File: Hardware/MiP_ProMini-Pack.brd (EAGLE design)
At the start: 41.4 x 63.8 mm, 45 parts, among them Q1 8MHz, U1 ATMEGA328, U2 MIC5205, U3 TS3USB221A

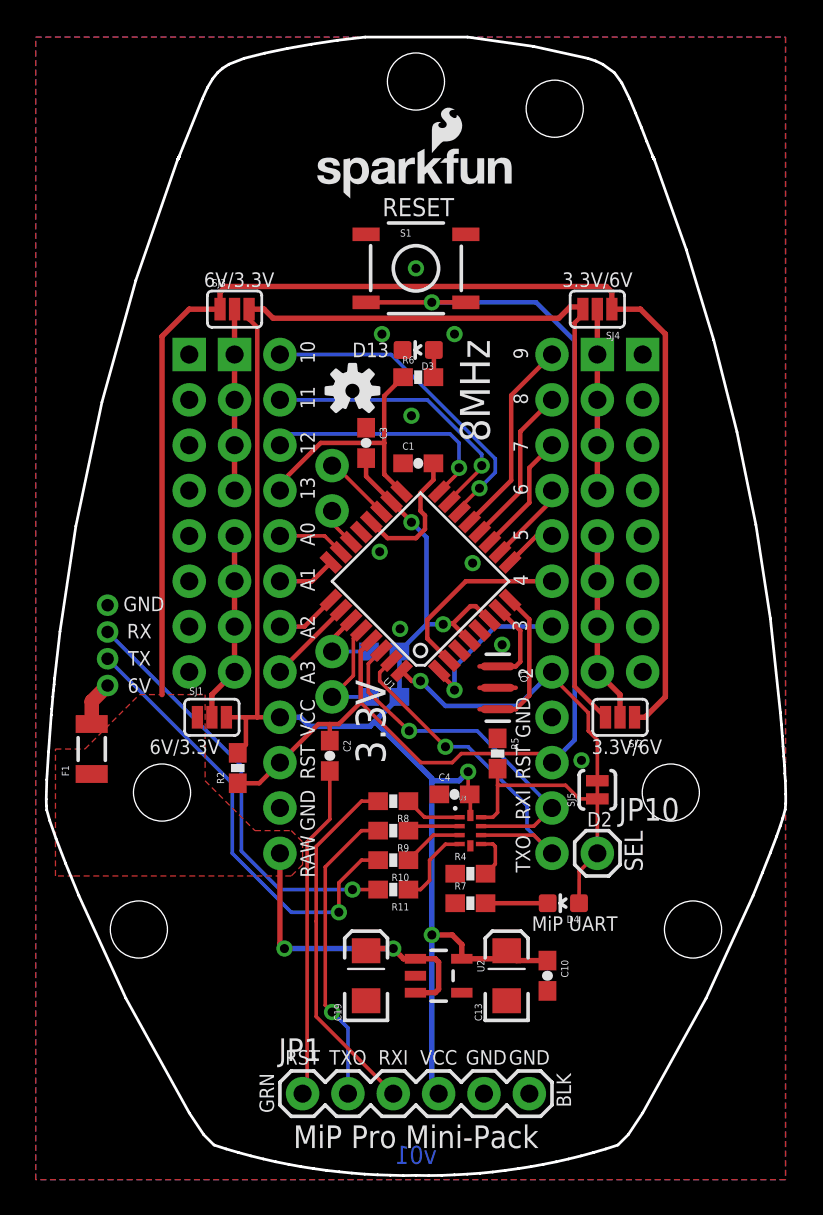
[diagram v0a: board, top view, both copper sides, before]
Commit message: moved components near screw holes. Gives more clearance for hardware
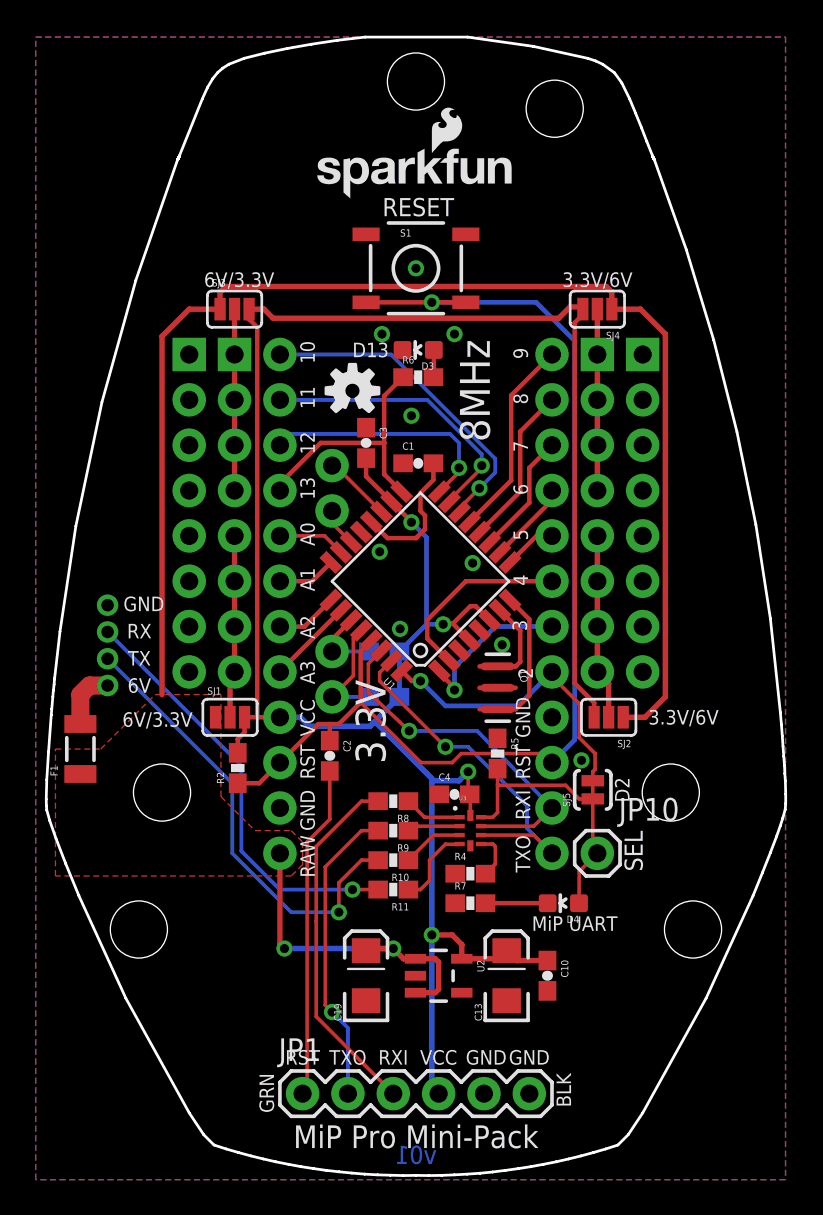
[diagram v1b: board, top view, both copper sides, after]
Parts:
- moved SJ1 1.02 mm to (10.9, 25.9)
- moved F1 0.63 mm to (2.54, 24.1)
- moved SJ2 0.63 mm to (32.1, 25.9)
- moved SJ5 0.25 mm to (31.2, 21.8)
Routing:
- net VCC: track 134.8 -> 133.5 mm
- net N$17: track 2.52 -> 3.38 mm
- net VIN: track 93.0 -> 93.6 mm
